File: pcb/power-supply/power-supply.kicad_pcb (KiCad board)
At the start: 2 copper layers, 32 parts, among them J1 Conn_01x20_Female, J10 Pwr_Terminal, J11 Pwr_Terminal, J12 Pwr_Terminal, J13 Conn_02x05, J14 Conn_02x05, J2 Conn_01x20_Female, J3 Conn_02x03, J4 Conn_01x03, J5 Conn_01x02, J6 Conn_01x02, J7 Conn_01x02, J8 Conn_01x02, J9 Pwr_Terminal, U1 Teensy++2.0

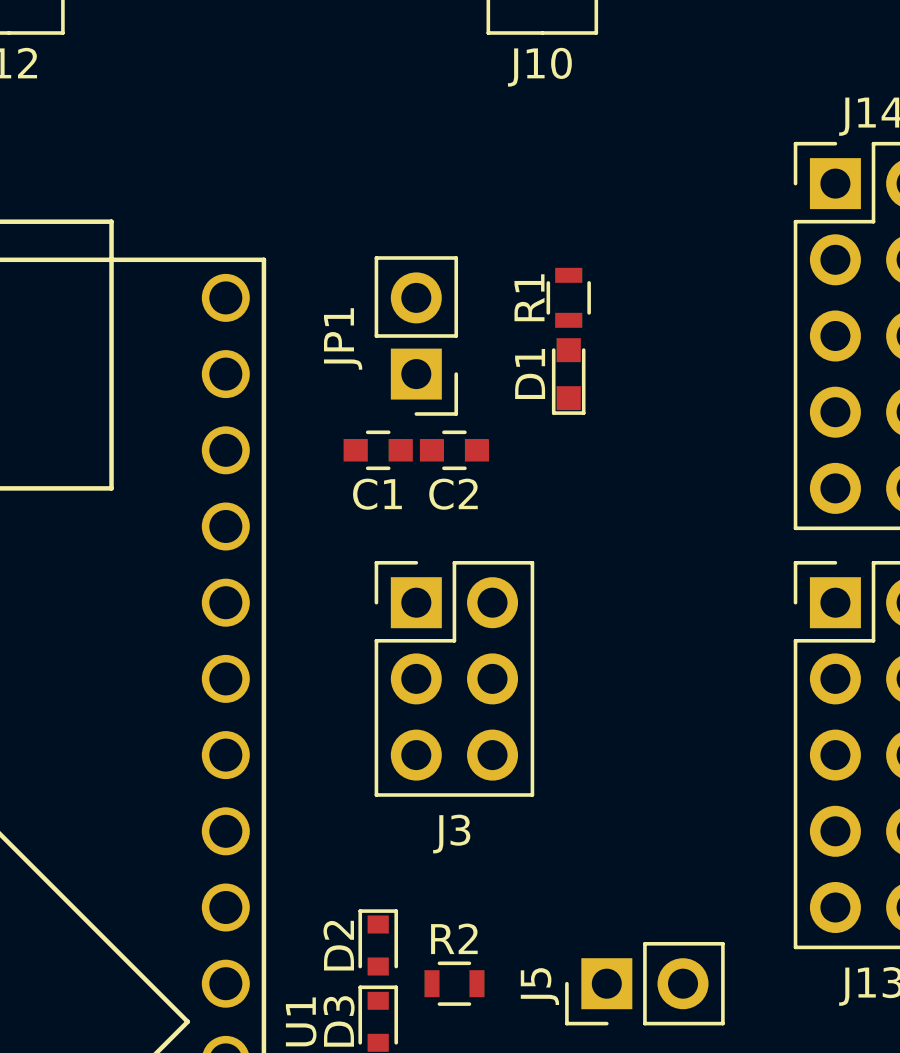
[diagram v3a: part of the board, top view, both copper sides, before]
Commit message: changed the 02x03 spi connector to a 02x05 connector with \CS
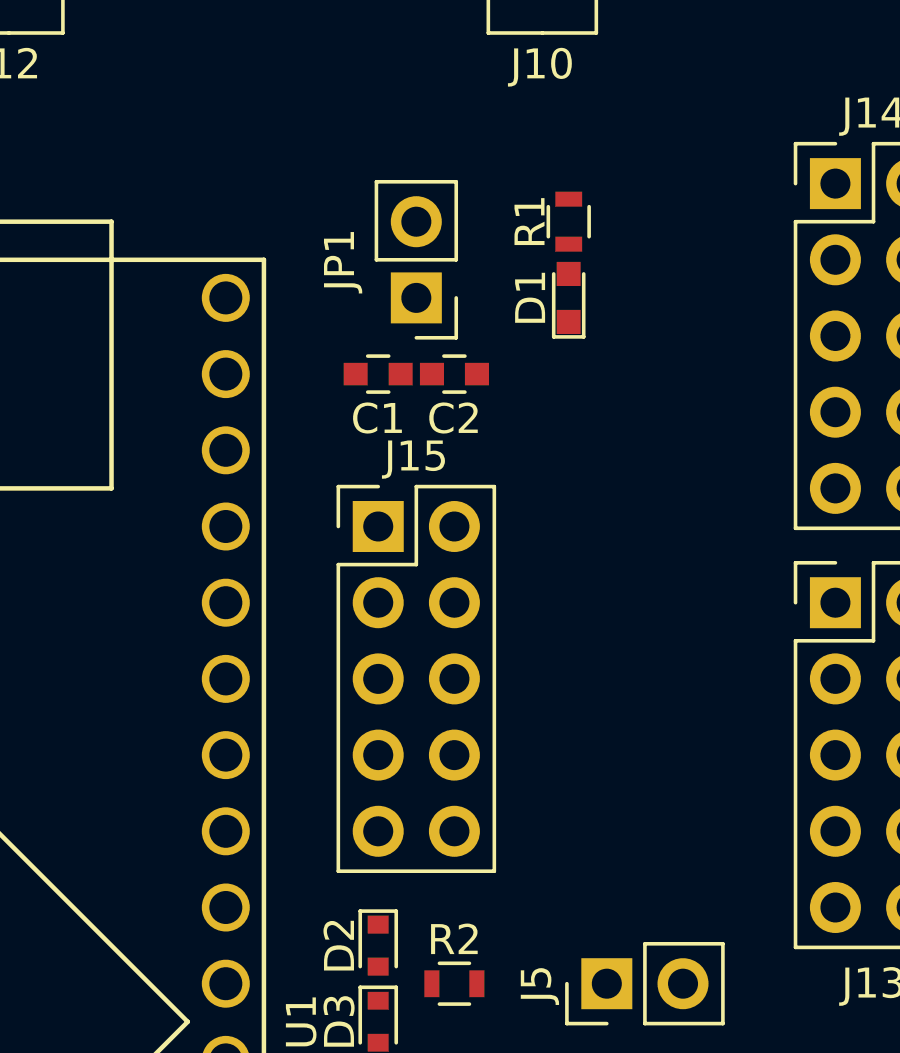
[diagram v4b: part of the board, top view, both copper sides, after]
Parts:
- removed J3: Conn_02x03, Pin_Headers:Pin_Header_Straight_2x03_Pitch2.54mm
- added J15: Conn_02x05, Pin_Headers:Pin_Header_Straight_2x05_Pitch2.54mm, F.Cu at (134.6, 119.4)
- moved C1 2.54 mm to (134.6, 114.3)
- moved C2 2.54 mm to (137.2, 114.3)
- moved R1 2.54 mm to (141.0, 109.2)
- moved D1 2.54 mm to (141.0, 111.8)
- moved JP1 2.54 mm to (135.9, 111.8)
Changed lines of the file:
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@@
 (kicad_pcb (version 4) (host pcbnew 4.0.7)
   (general
-    (links 46)
-    (no_connects 46)
-    (area 0 0 0 0)
+    (links 49)
+    (no_connects 49)
+    (area 77.294761 89.005 155.87762 163.425)
     (thickness 1.6)
     (drawings 0)
@@
     (zones 0)
     (modules 32)
-    (nets 134)
+    (nets 135)
   )
   (page A4)
@@
   (net 132 "Net-(U1-Pad51)")
   (net 133 "Net-(U1-Pad52)")
+  (net 134 /~RST)
   (net_class Default "This is the default net class."
     (clearance 0.2)
@@
     (add_net /F7)
     (add_net /VREF)
+    (add_net /~RST)
     (add_net GND)
     (add_net "Net-(C1-Pad1)")
@@
   )
   (module Capacitors_SMD:C_0603 (layer F.Cu)
-    (at 134.62 116.84 180)
+    (at 134.62 114.3 180)
     (descr "Capacitor SMD 0603, reflow soldering, AVX (see smccp.pdf)")
     (tags "capacitor 0603")
@@
   )
   (module Capacitors_SMD:C_0603 (layer F.Cu)
-    (at 137.16 116.84 180)
+    (at 137.16 114.3 180)
     (descr "Capacitor SMD 0603, reflow soldering, AVX (see smccp.pdf)")
     (tags "capacitor 0603")
@@
   )
   (module Pin_Headers:Pin_Header_Straight_1x02_Pitch2.54mm (layer F.Cu)
-    (at 135.89 114.3 180)
+    (at 135.89 111.76 180)
     (descr "Through hole straight pin header, 1x02, 2.54mm pitch, single row")
     (tags "Through hole pin header THT 1x02 2.54mm single row")
@@
   )
   (module Resistors_SMD:R_0603 (layer F.Cu)
-    (at 140.97 111.76 270)
+    (at 140.97 109.22 270)
     (descr "Resistor SMD 0603, reflow soldering, Vishay (see dcrcw.pdf)")
     (tags "resistor 0603")
@@
   )
   (module LEDs:LED_0603 (layer F.Cu)
-    (at 140.97 114.3 90)
+    (at 140.97 111.76 90)
     (descr "LED 0603 smd package")
     (tags "LED led 0603 SMD smd SMT smt smdled SMDLED smtled SMTLED")
@@
       (scale (xyz 1 1 1))
       (rotate (xyz 0 0 270))
-    )
-  )
-  (module Pin_Headers:Pin_Header_Straight_2x03_Pitch2.54mm (layer F.Cu)
-    (at 135.89 121.92)
-    (descr "Through hole straight pin header, 2x03, 2.54mm pitch, double rows")
-    (tags "Through hole pin header THT 2x03 2.54mm double row")
-    (fp_text reference J3 (at 1.27 7.62) (layer F.SilkS)
-      (effects (font (size 1 1) (thickness 0.15)))
-    )
-    (fp_text value Conn_02x03 (at 1.27 7.41) (layer F.Fab)
-      (effects (font (size 1 1) (thickness 0.15)))
-    )
-    (fp_line (start 0 -1.27) (end 3.81 -1.27) (layer F.Fab) (width 0.1))
-    (fp_line (start 3.81 -1.27) (end 3.81 6.35) (layer F.Fab) (width 0.1))
-    (fp_line (start 3.81 6.35) (end -1.27 6.35) (layer F.Fab) (width 0.1))
-    (fp_line (start -1.27 6.35) (end -1.27 0) (layer F.Fab) (width 0.1))
-    (fp_line (start -1.27 0) (end 0 -1.27) (layer F.Fab) (width 0.1))
-    (fp_line (start -1.33 6.41) (end 3.87 6.41) (layer F.SilkS) (width 0.12))
-    (fp_line (start -1.33 1.27) (end -1.33 6.41) (layer F.SilkS) (width 0.12))
-    (fp_line (start 3.87 -1.33) (end 3.87 6.41) (layer F.SilkS) (width 0.12))
-    (fp_line (start -1.33 1.27) (end 1.27 1.27) (layer F.SilkS) (width 0.12))
-    (fp_line (start 1.27 1.27) (end 1.27 -1.33) (layer F.SilkS) (width 0.12))
-    (fp_line (start 1.27 -1.33) (end 3.87 -1.33) (layer F.SilkS) (width 0.12))
-    (fp_line (start -1.33 0) (end -1.33 -1.33) (layer F.SilkS) (width 0.12))
-    (fp_line (start -1.33 -1.33) (end 0 -1.33) (layer F.SilkS) (width 0.12))
-    (fp_line (start -1.8 -1.8) (end -1.8 6.85) (layer F.CrtYd) (width 0.05))
-    (fp_line (start -1.8 6.85) (end 4.35 6.85) (layer F.CrtYd) (width 0.05))
-    (fp_line (start 4.35 6.85) (end 4.35 -1.8) (layer F.CrtYd) (width 0.05))
-    (fp_line (start 4.35 -1.8) (end -1.8 -1.8) (layer F.CrtYd) (width 0.05))
-    (fp_text user %R (at 1.27 2.54 90) (layer F.Fab)
-      (effects (font (size 1 1) (thickness 0.15)))
-    )
-    (pad 1 thru_hole rect (at 0 0) (size 1.7 1.7) (drill 1) (layers *.Cu *.Mask)
-      (net 31 /B3))
-    (pad 2 thru_hole oval (at 2.54 0) (size 1.7 1.7) (drill 1) (layers *.Cu *.Mask)
-      (net 4 +5V))
-    (pad 3 thru_hole oval (at 0 2.54) (size 1.7 1.7) (drill 1) (layers *.Cu *.Mask)
-      (net 33 /B1))
-    (pad 4 thru_hole oval (at 2.54 2.54) (size 1.7 1.7) (drill 1) (layers *.Cu *.Mask)
-      (net 32 /B2))
-    (pad 5 thru_hole oval (at 0 5.08) (size 1.7 1.7) (drill 1) (layers *.Cu *.Mask)
-      (net 34 /B0))
-    (pad 6 thru_hole oval (at 2.54 5.08) (size 1.7 1.7) (drill 1) (layers *.Cu *.Mask)
-      (net 2 GND))
-    (model ${KISYS3DMOD}/Pin_Headers.3dshapes/Pin_Header_Straight_2x03_Pitch2.54mm.wrl
-      (at (xyz 0 0 0))
-      (scale (xyz 1 1 1))
-      (rotate (xyz 0 0 0))
     )
   )
@@
       (net 133 "Net-(U1-Pad52)"))
   )
+  (module Pin_Headers:Pin_Header_Straight_2x05_Pitch2.54mm (layer F.Cu)
+    (at 134.62 119.38)
+    (descr "Through hole straight pin header, 2x05, 2.54mm pitch, double rows")
+    (tags "Through hole pin header THT 2x05 2.54mm double row")
+    (fp_text reference J15 (at 1.27 -2.33) (layer F.SilkS)
+      (effects (font (size 1 1) (thickness 0.15)))
+    )
+    (fp_text value Conn_02x05 (at 1.27 12.49) (layer F.Fab)
+      (effects (font (size 1 1) (thickness 0.15)))
+    )
+    (fp_line (start 0 -1.27) (end 3.81 -1.27) (layer F.Fab) (width 0.1))
+    (fp_line (start 3.81 -1.27) (end 3.81 11.43) (layer F.Fab) (width 0.1))
+    (fp_line (start 3.81 11.43) (end -1.27 11.43) (layer F.Fab) (width 0.1))
+    (fp_line (start -1.27 11.43) (end -1.27 0) (layer F.Fab) (width 0.1))
+    (fp_line (start -1.27 0) (end 0 -1.27) (layer F.Fab) (width 0.1))
+    (fp_line (start -1.33 11.49) (end 3.87 11.49) (layer F.SilkS) (width 0.12))
+    (fp_line (start -1.33 1.27) (end -1.33 11.49) (layer F.SilkS) (width 0.12))
+    (fp_line (start 3.87 -1.33) (end 3.87 11.49) (layer F.SilkS) (width 0.12))
+    (fp_line (start -1.33 1.27) (end 1.27 1.27) (layer F.SilkS) (width 0.12))
+    (fp_line (start 1.27 1.27) (end 1.27 -1.33) (layer F.SilkS) (width 0.12))
+    (fp_line (start 1.27 -1.33) (end 3.87 -1.33) (layer F.SilkS) (width 0.12))
+    (fp_line (start -1.33 0) (end -1.33 -1.33) (layer F.SilkS) (width 0.12))
+    (fp_line (start -1.33 -1.33) (end 0 -1.33) (layer F.SilkS) (width 0.12))
+    (fp_line (start -1.8 -1.8) (end -1.8 11.95) (layer F.CrtYd) (width 0.05))
+    (fp_line (start -1.8 11.95) (end 4.35 11.95) (layer F.CrtYd) (width 0.05))
+    (fp_line (start 4.35 11.95) (end 4.35 -1.8) (layer F.CrtYd) (width 0.05))
+    (fp_line (start 4.35 -1.8) (end -1.8 -1.8) (layer F.CrtYd) (width 0.05))
+    (fp_text user %R (at 1.27 5.08 90) (layer F.Fab)
+      (effects (font (size 1 1) (thickness 0.15)))
+    )
+    (pad 1 thru_hole rect (at 0 0) (size 1.7 1.7) (drill 1) (layers *.Cu *.Mask)
+      (net 32 /B2))
+    (pad 2 thru_hole oval (at 2.54 0) (size 1.7 1.7) (drill 1) (layers *.Cu *.Mask)
+      (net 4 +5V))
+    (pad 3 thru_hole oval (at 0 2.54) (size 1.7 1.7) (drill 1) (layers *.Cu *.Mask)
+      (net 34 /B0))
+    (pad 4 thru_hole oval (at 2.54 2.54) (size 1.7 1.7) (drill 1) (layers *.Cu *.Mask)
+      (net 2 GND))
+    (pad 5 thru_hole oval (at 0 5.08) (size 1.7 1.7) (drill 1) (layers *.Cu *.Mask)
+      (net 134 /~RST))
+    (pad 6 thru_hole oval (at 2.54 5.08) (size 1.7 1.7) (drill 1) (layers *.Cu *.Mask)
+      (net 2 GND))
+    (pad 7 thru_hole oval (at 0 7.62) (size 1.7 1.7) (drill 1) (layers *.Cu *.Mask)
+      (net 33 /B1))
+    (pad 8 thru_hole oval (at 2.54 7.62) (size 1.7 1.7) (drill 1) (layers *.Cu *.Mask)
+      (net 2 GND))
+    (pad 9 thru_hole oval (at 0 10.16) (size 1.7 1.7) (drill 1) (layers *.Cu *.Mask)
+      (net 31 /B3))
+    (pad 10 thru_hole oval (at 2.54 10.16) (size 1.7 1.7) (drill 1) (layers *.Cu *.Mask)
+      (net 2 GND))
+    (model ${KISYS3DMOD}/Pin_Headers.3dshapes/Pin_Header_Straight_2x05_Pitch2.54mm.wrl
+      (at (xyz 0 0 0))
+      (scale (xyz 1 1 1))
+      (rotate (xyz 0 0 0))
+    )
+  )
 )
